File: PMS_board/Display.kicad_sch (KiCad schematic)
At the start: 5 parts, among them Q1 BSS138

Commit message: Finish Schematic
There's definitely stuff I missed, but I'm tired so we can review later. For my members to keep track of things, these are the changes/last minute additions I ran out of time to teach:
- brake chopper circuitry & reverse voltage protection for aux & motor rails
- microcontroller pinnouts
- net connections between sheets
- voltage resistors & system voltage measurements
- cell sense connectors & switch
- ADC routing
Please Please PLEASE ask questions about these additions. I don't want you guys to feel like you don't own this schematic, and I'm sorry I had to take away some of these designs to finish early. I definitely left too much on your plate to get everything perfect, which is my bad. I will happily walk through each and every circuit and help explain each part so you can better know your project when we get to reviewing and debugging later down the line.
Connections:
- net LCDpin3: now reaches LCD1.10 (DB3)
- net LCDpin4: now reaches LCD1.11 (DB4)
- net LCDpin5: now reaches LCD1.12 (DB5)
- net LCDpin6: now reaches LCD1.13 (DB6)
- net LCDpin7: now reaches LCD1.14 (DB7)
- net LCDpin0: now reaches LCD1.7 (DB0)
- net LCDpin1: now reaches LCD1.8 (DB1)
- net LCDpin2: now reaches LCD1.9 (DB2)
- net BuzzerSignal renamed Buzzer_Signal
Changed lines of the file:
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@@
 		(color 0 0 0 0)
 	)
-	(bus_entry
-		(at 71.12 134.62)
-		(size 2.54 2.54)
-		(stroke
-			(width 0)
-			(type default)
-		)
-	)
-	(bus_entry
-		(at 71.12 121.92)
-		(size 2.54 2.54)
-		(stroke
-			(width 0)
-			(type default)
-		)
-	)
-	(bus_entry
-		(at 71.12 116.84)
-		(size 2.54 2.54)
-		(stroke
-			(width 0)
-			(type default)
-		)
-	)
-	(bus_entry
-		(at 71.12 127)
-		(size 2.54 2.54)
-		(stroke
-			(width 0)
-			(type default)
-		)
-	)
-	(bus_entry
-		(at 71.12 119.38)
-		(size 2.54 2.54)
-		(stroke
-			(width 0)
-			(type default)
-		)
-	)
-	(bus_entry
-		(at 71.12 129.54)
-		(size 2.54 2.54)
-		(stroke
-			(width 0)
-			(type default)
-		)
-	)
-	(bus_entry
-		(at 71.12 124.46)
-		(size 2.54 2.54)
-		(stroke
-			(width 0)
-			(type default)
-		)
-	)
-	(bus_entry
-		(at 71.12 132.08)
-		(size 2.54 2.54)
-		(stroke
-			(width 0)
-			(type default)
-		)
-	)
 	(wire
 		(pts
@@
 	(wire
 		(pts
+			(xy 72.39 134.62) (xy 73.66 134.62)
+		)
+		(stroke
+			(width 0)
+			(type default)
+		)
+	)
+	(wire
+		(pts
 			(xy 106.68 132.08) (xy 106.68 133.35)
 		)
@@
 	(wire
 		(pts
+			(xy 138.43 120.65) (xy 146.05 120.65)
+		)
+		(stroke
+			(width 0)
+			(type default)
+		)
+	)
+	(wire
+		(pts
 			(xy 162.56 121.92) (xy 162.56 114.3)
 		)
@@
 	(wire
 		(pts
+			(xy 72.39 132.08) (xy 73.66 132.08)
+		)
+		(stroke
+			(width 0)
+			(type default)
+		)
+	)
+	(wire
+		(pts
 			(xy 156.21 109.22) (xy 156.21 107.95)
 		)
@@
 	(wire
 		(pts
+			(xy 72.39 137.16) (xy 73.66 137.16)
+		)
+		(stroke
+			(width 0)
+			(type default)
+		)
+	)
+	(wire
+		(pts
 			(xy 106.68 129.54) (xy 104.14 129.54)
 		)
@@
 	(wire
 		(pts
+			(xy 72.39 124.46) (xy 73.66 124.46)
+		)
+		(stroke
+			(width 0)
+			(type default)
+		)
+	)
+	(wire
+		(pts
 			(xy 186.69 113.03) (xy 186.69 109.22)
 		)
@@
 		)
 	)
-	(bus
-		(pts
-			(xy 66.04 116.84) (xy 71.12 116.84)
-		)
-		(stroke
-			(width 0)
-			(type default)
-		)
-	)
-	(bus
-		(pts
-			(xy 71.12 134.62) (xy 71.12 116.84)
+	(wire
+		(pts
+			(xy 72.39 119.38) (xy 73.66 119.38)
 		)
 		(stroke
@@
 	(wire
 		(pts
-			(xy 130.81 120.65) (xy 146.05 120.65)
+			(xy 72.39 129.54) (xy 73.66 129.54)
+		)
+		(stroke
+			(width 0)
+			(type default)
+		)
+	)
+	(wire
+		(pts
+			(xy 72.39 127) (xy 73.66 127)
 		)
 		(stroke
@@
 		)
 	)
-	(label "BuzzerSignal"
-		(at 130.81 120.65 0)
-		(effects
-			(font
-				(size 1.27 1.27)
-			)
-			(justify left bottom)
+	(wire
+		(pts
+			(xy 72.39 121.92) (xy 73.66 121.92)
+		)
+		(stroke
+			(width 0)
+			(type default)
+		)
+	)
+	(hierarchical_label "LCDpin3"
+		(shape tri_state)
+		(at 72.39 127 180)
+		(effects
+			(font
+				(size 1.27 1.27)
+			)
+			(justify right)
+		)
+	)
+	(hierarchical_label "LCDpin2"
+		(shape tri_state)
+		(at 72.39 124.46 180)
+		(effects
+			(font
+				(size 1.27 1.27)
+			)
+			(justify right)
+		)
+	)
+	(hierarchical_label "LCDpin7"
+		(shape tri_state)
+		(at 72.39 137.16 180)
+		(effects
+			(font
+				(size 1.27 1.27)
+			)
+			(justify right)
+		)
+	)
+	(hierarchical_label "LCDpin5"
+		(shape tri_state)
+		(at 72.39 132.08 180)
+		(effects
+			(font
+				(size 1.27 1.27)
+			)
+			(justify right)
+		)
+	)
+	(hierarchical_label "LCDpin6"
+		(shape tri_state)
+		(at 72.39 134.62 180)
+		(effects
+			(font
+				(size 1.27 1.27)
+			)
+			(justify right)
+		)
+	)
+	(hierarchical_label "LCDpin0"
+		(shape tri_state)
+		(at 72.39 119.38 180)
+		(effects
+			(font
+				(size 1.27 1.27)
+			)
+			(justify right)
 		)
 	)
@@
 		)
 	)
-	(hierarchical_label "D[0..7]"
-		(shape bidirectional)
-		(at 66.04 116.84 180)
+	(hierarchical_label "Buzzer_Signal"
+		(shape input)
+		(at 138.43 120.65 180)
+		(effects
+			(font
+				(size 1.27 1.27)
+			)
+			(justify right)
+		)
+	)
+	(hierarchical_label "LCDpin1"
+		(shape tri_state)
+		(at 72.39 121.92 180)
 		(effects
 			(font
@@
 		)
 	)
+	(hierarchical_label "LCDpin4"
+		(shape tri_state)
+		(at 72.39 129.54 180)
+		(effects
+			(font
+				(size 1.27 1.27)
+			)
+			(justify right)
+		)
+	)
 	(hierarchical_label "RW"
-		(shape input)
+		(shape bidirectional)
 		(at 73.66 111.76 180)
 		(effects

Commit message: Add Footprints & such
whoops forgot to push yesterday teehee
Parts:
- B1: footprint (none) -> Buzzer_Beeper:Buzzer_12x9.5RM7.6
- D9: footprint (none) -> LED_SMD:LED_0603_1608Metric
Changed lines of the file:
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@@
 			)
 		)
-		(property "Footprint" ""
+		(property "Footprint" "Buzzer_Beeper:Buzzer_12x9.5RM7.6"
 			(at 151.13 102.87 0)
 			(hide yes)
@@
 			)
 		)
-		(property "Footprint" ""
+		(property "Footprint" "LED_SMD:LED_0603_1608Metric"
 			(at 175.26 121.92 0)
 			(hide yes)

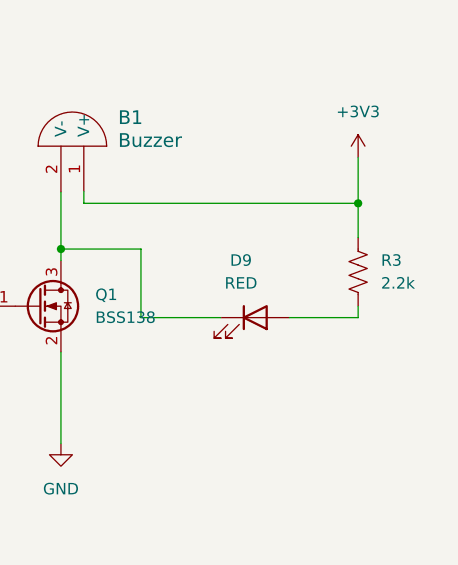
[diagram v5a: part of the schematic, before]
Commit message: Minor component tweaks and added a seperate LED sheet
Changed component values
Added labels
Moved LEDs to it's own sheet
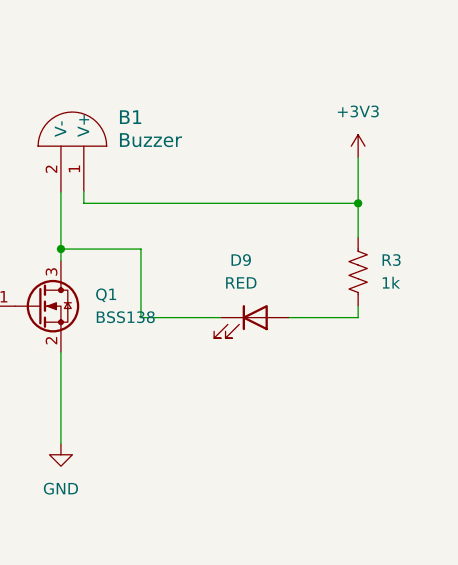
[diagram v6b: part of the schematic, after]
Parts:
- R3: value 2.2k -> 1k
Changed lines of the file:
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@@
 			)
 		)
-		(property "Value" "2.2k"
+		(property "Value" "1k"
 			(at 189.23 118.1099 0)
 			(show_name no)

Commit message: How did our footprints get this geeked???
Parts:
- D9: footprint LED_SMD:LED_0603_1608Metric -> (none)
- R3: footprint (none) -> Resistor_SMD:R_0603_1608Metric_Pad0.98x0.95mm_HandSolder
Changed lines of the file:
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@@
 			)
 		)
-		(property "Footprint" ""
+		(property "Footprint" "Resistor_SMD:R_0603_1608Metric_Pad0.98x0.95mm_HandSolder"
 			(at 187.706 117.094 90)
 			(hide yes)
@@
 			)
 		)
-		(property "Footprint" "LED_SMD:LED_0603_1608Metric"
+		(property "Footprint" ""
 			(at 175.26 121.92 0)
 			(hide yes)

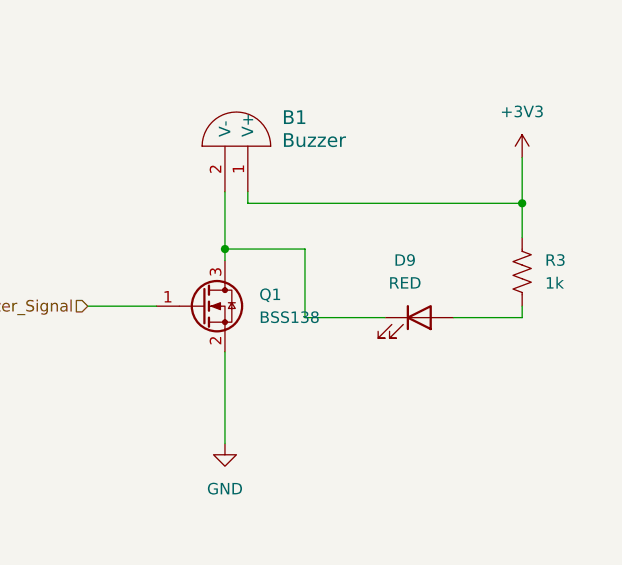
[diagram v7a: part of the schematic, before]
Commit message: Footprints and naming things
Changed component names to be a bit more representitive

Some minor footprints
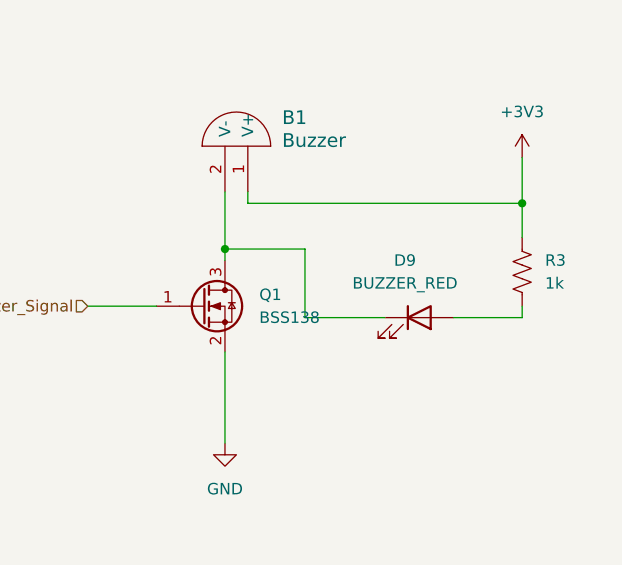
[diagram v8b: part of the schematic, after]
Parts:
- B1: footprint Buzzer_Beeper:Buzzer_12x9.5RM7.6 -> (none)
- D9: value RED -> BUZZER_RED
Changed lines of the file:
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@@
 			)
 		)
-		(property "Footprint" "Buzzer_Beeper:Buzzer_12x9.5RM7.6"
+		(property "Footprint" ""
 			(at 151.13 102.87 0)
 			(hide yes)
@@
 			)
 		)
-		(property "Value" "RED"
+		(property "Value" "BUZZER_RED"
 			(at 173.6725 118.11 0)
 			(show_name no)
